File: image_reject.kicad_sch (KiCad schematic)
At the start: 58 parts, among them Q11 Q_PMOS_GSD, Q12 BFR840, Q13 Q_PMOS_GSD, Q2 BFP840, U1 MXD8546F, U38 74LVC1G00, U39 74LVC1G00, U9 BGS13SN8

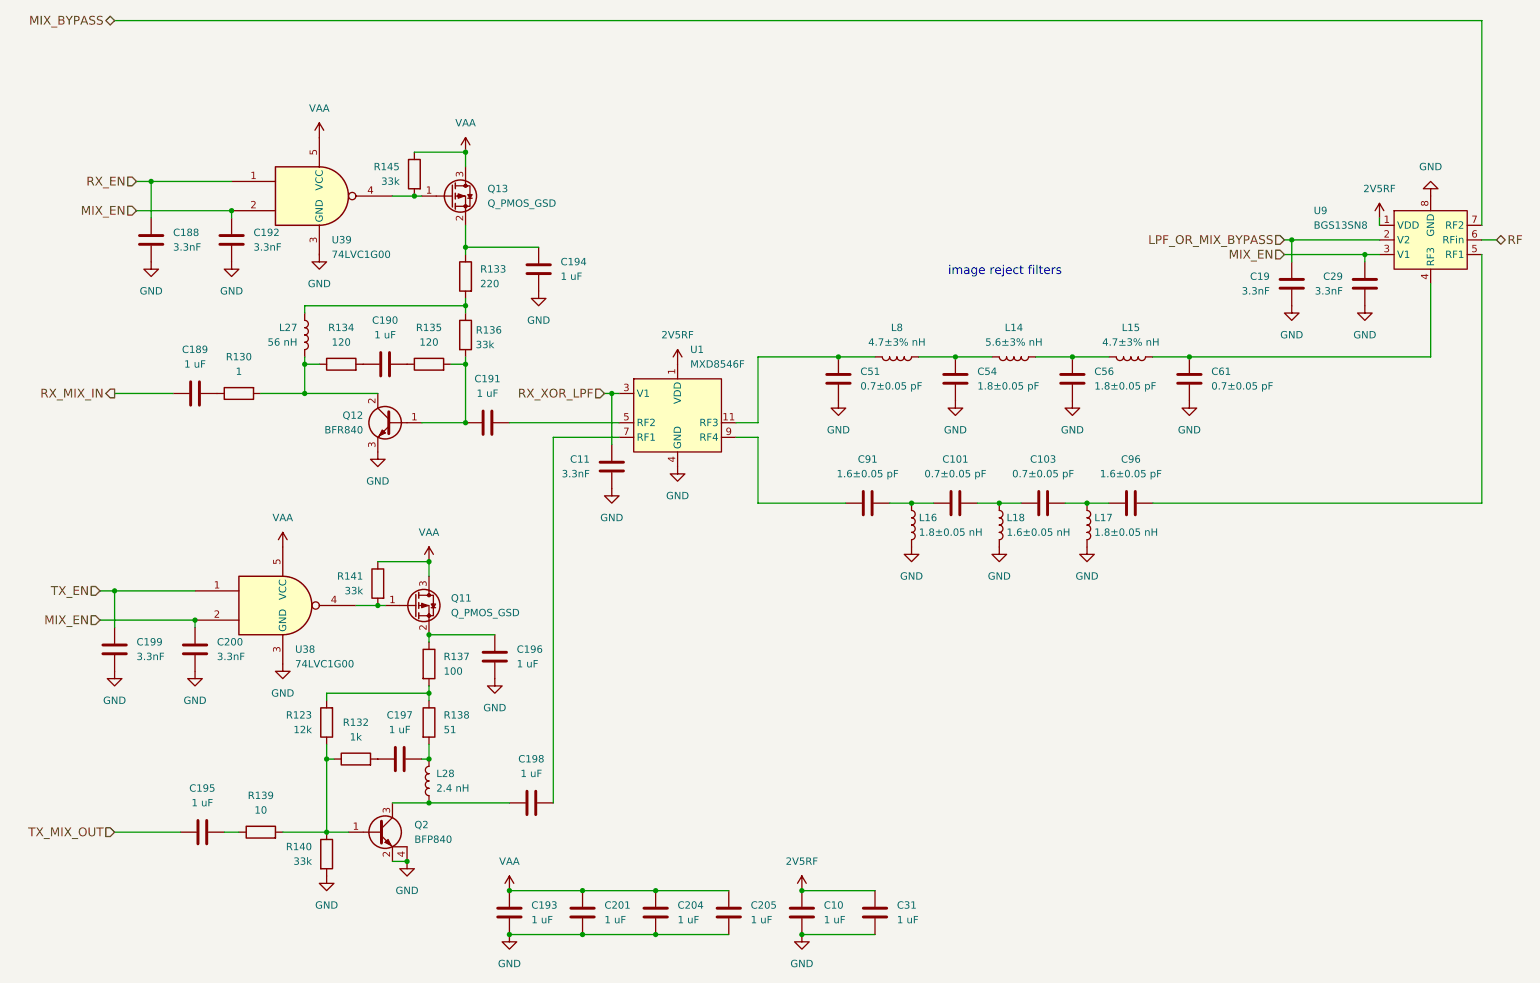
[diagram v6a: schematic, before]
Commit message: Replace mixer compensation amps with single BGB741
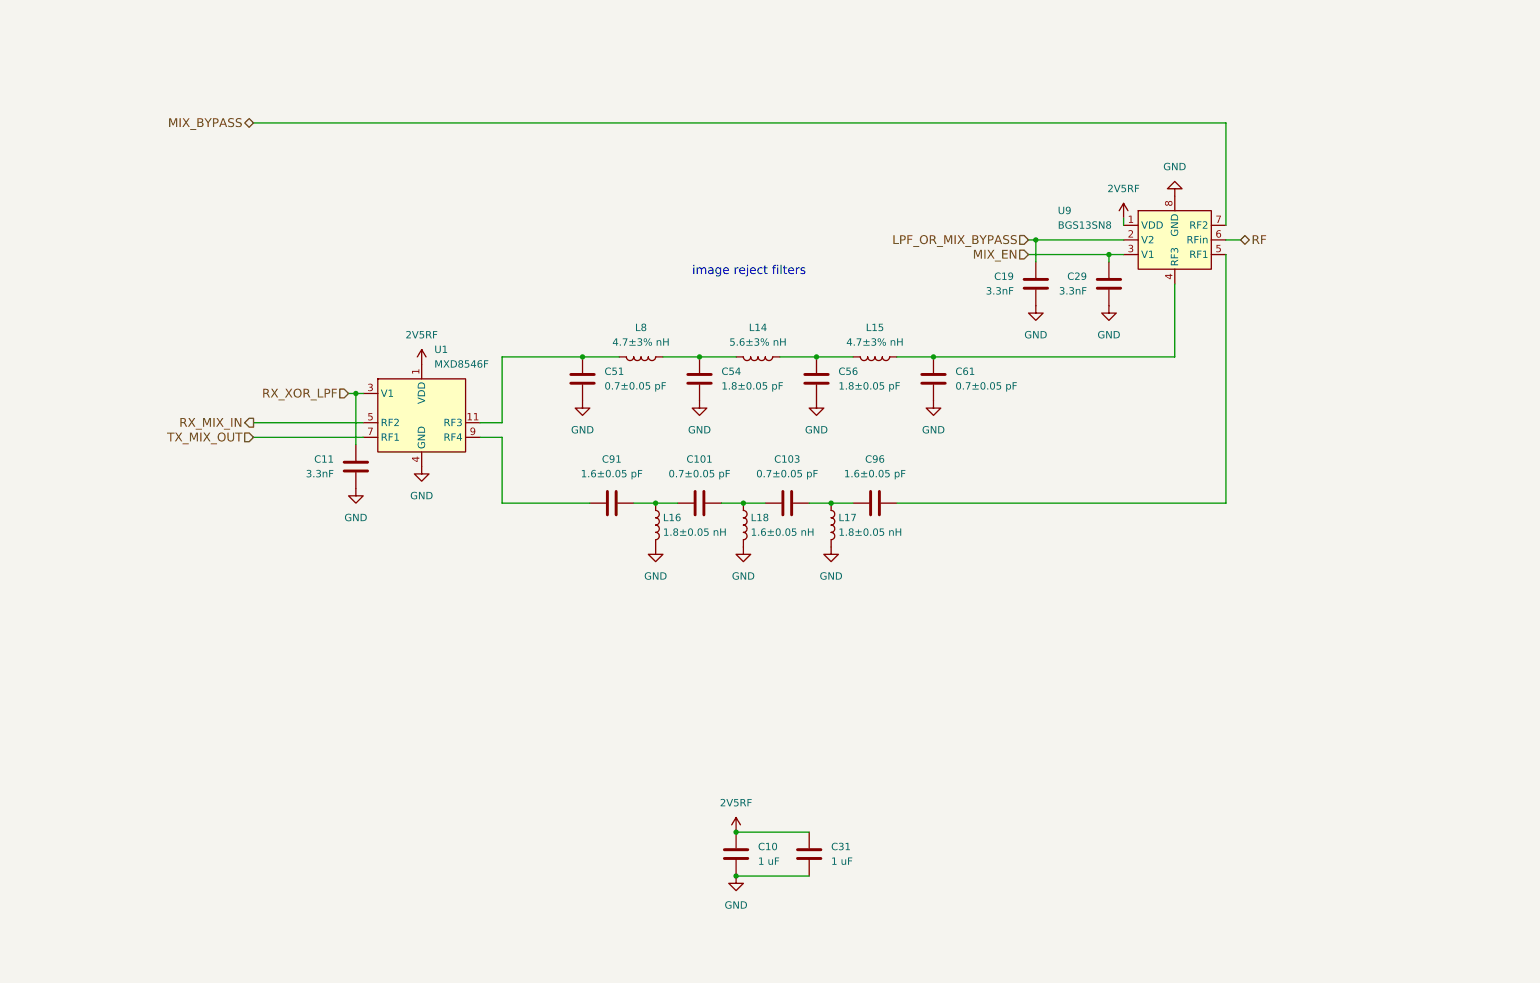
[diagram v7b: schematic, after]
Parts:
- removed C188, C192, C199, C200: 3.3nF, Capacitor_SMD:C_0201_0603Metric, symbol Device:C
- removed C189, C190, C191, C193, C194, C195, C196, C197, C198, C201, C204, C205: 1 uF, Capacitor_SMD:C_0201_0603Metric, symbol Device:C
- removed L27: 56 nH, Inductor_SMD:L_0201_0603Metric, symbol Device:L
- removed L28: 2.4 nH, Inductor_SMD:L_0201_0603Metric, symbol Device:L
- removed Q11, Q13: Q_PMOS_GSD, praline:TSLP-3-9, symbol Transistor_FET:Q_PMOS_GSD
- removed Q12: BFR840, praline:TSLP-3-9, symbol Transistor_BJT:Q_NPN_BCE
- removed Q2: BFP840, praline:SOT-343-4-3, symbol praline:Q_NPN_BECE
- removed R123: 12k, Resistor_SMD:R_0201_0603Metric, symbol Device:R
- removed R130: 1, Resistor_SMD:R_0201_0603Metric, symbol Device:R
- removed R132: 1k, Resistor_SMD:R_0201_0603Metric, symbol Device:R
- removed R133: 220, Resistor_SMD:R_0201_0603Metric, symbol Device:R
- removed R134, R135: 120, Resistor_SMD:R_0201_0603Metric, symbol Device:R
- removed R136, R140, R141, R145: 33k, Resistor_SMD:R_0201_0603Metric, symbol Device:R
- removed R137: 100, Resistor_SMD:R_0201_0603Metric, symbol Device:R
- removed R138: 51, Resistor_SMD:R_0201_0603Metric, symbol Device:R
- removed R139: 10, Resistor_SMD:R_0201_0603Metric, symbol Device:R
- removed U38, U39: 74LVC1G00, Package_TO_SOT_SMD:SOT-353_SC-70-5, symbol 74xGxx:74LVC1G00
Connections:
- net RX_MIX_IN: now also U1.5 (RF2)
- net TX_MIX_OUT: now also U1.7 (RF1)
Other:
- moved on the sheet: C10, C101, C103, C11, C19, C29, C31, C51, C54, C56, C61, C91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

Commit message: Standardize component Value fields
Use Tolerance field instead of expressing tolerance in Value field
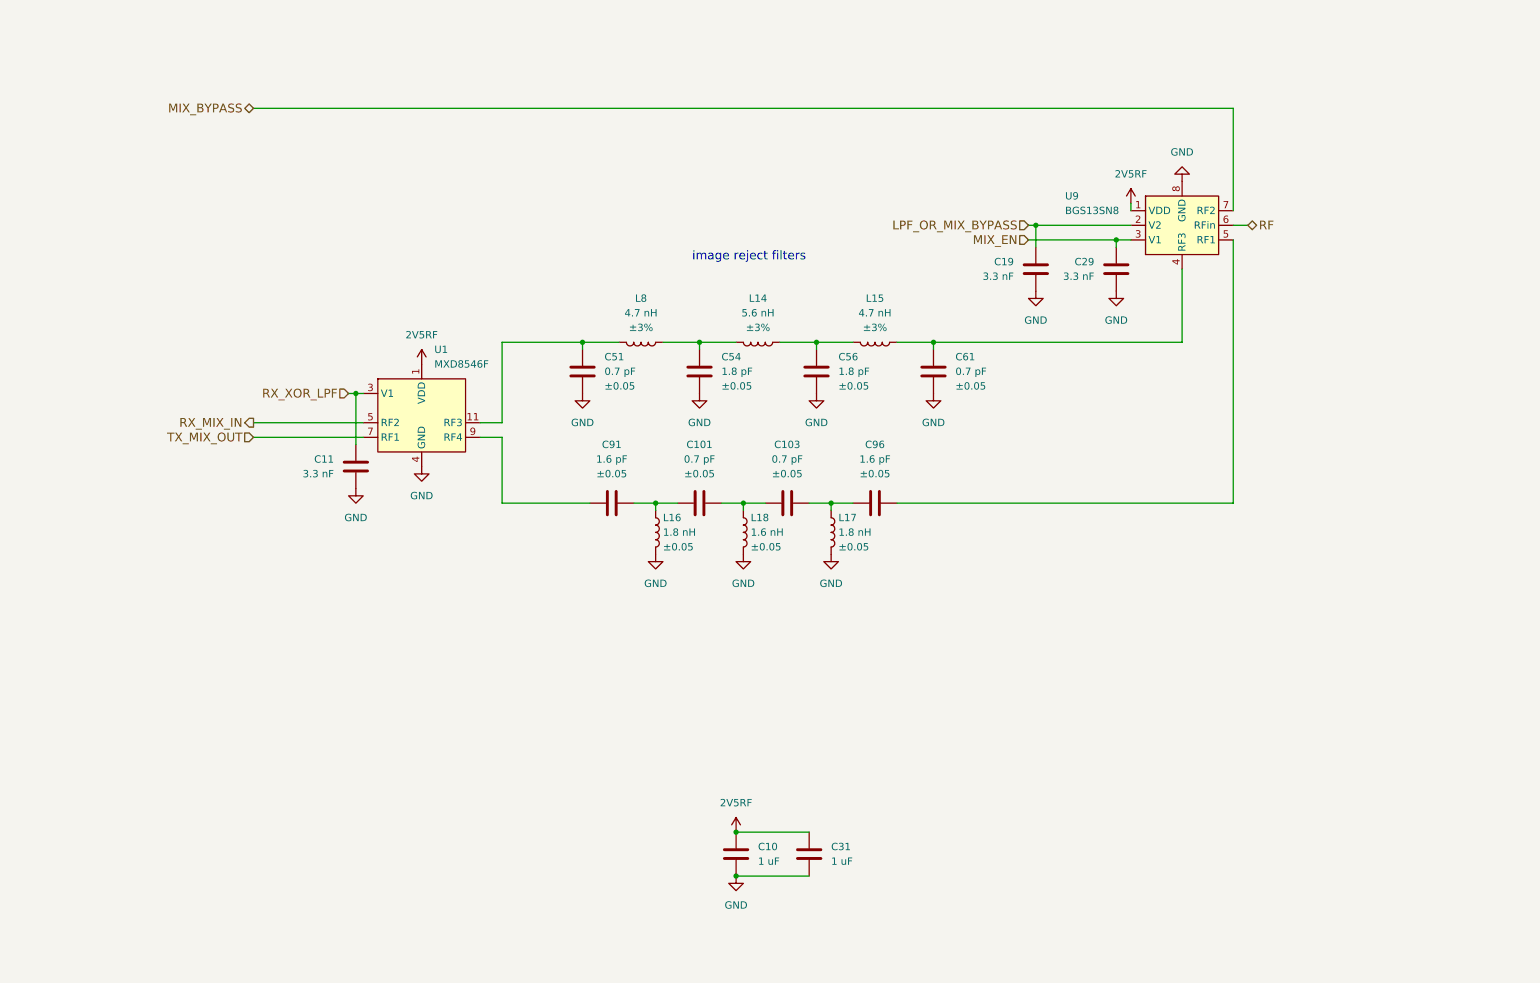
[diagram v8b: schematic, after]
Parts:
- C101, C103, C51, C61: value 0.7±0.05 pF -> 0.7 pF; Tolerance (none) -> ±0.05
- C11, C19, C29: value 3.3nF -> 3.3 nF
- C54, C56: value 1.8±0.05 pF -> 1.8 pF; Tolerance (none) -> ±0.05
- C91, C96: value 1.6±0.05 pF -> 1.6 pF; Tolerance (none) -> ±0.05
- L14: value 5.6±3% nH -> 5.6 nH; Tolerance (none) -> ±3%
- L15, L8: value 4.7±3% nH -> 4.7 nH; Tolerance (none) -> ±3%
- L16, L17: value 1.8±0.05 nH -> 1.8 nH; Tolerance (none) -> ±0.05
- L18: value 1.6±0.05 nH -> 1.6 nH; Tolerance (none) -> ±0.05
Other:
- moved on the sheet: C19, C29, C51, C54, C56, C61, L14, L15, L16, L17, L18, L8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
